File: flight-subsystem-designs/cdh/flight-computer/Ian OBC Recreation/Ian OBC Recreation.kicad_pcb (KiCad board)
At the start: 4 copper layers, 90 x 96 mm, 42 parts, among them J8 Conn_02x26_Odd_Even, Q1 AON6411, Q2 AON6411, U1 BEAGLEBONEBLACK, U2 TPS2400DBVR, U3 TCAN337G, U4 MCP7940N-xSN, U5 ADM3485EARZ, U6 MAX706RESA+T, U7 TMP36xS, U8 TPS2400DBVR

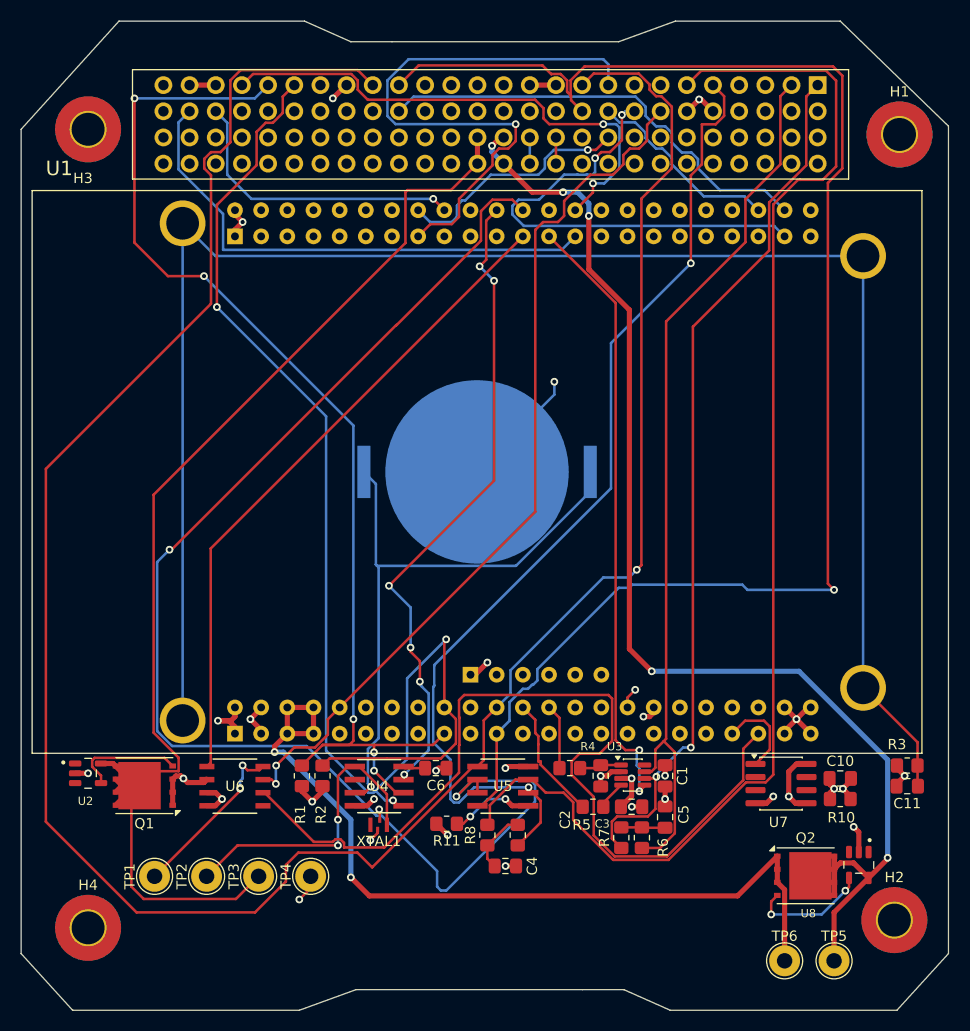
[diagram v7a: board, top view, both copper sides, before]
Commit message: Not LibreCube Friendly, Holes Removed
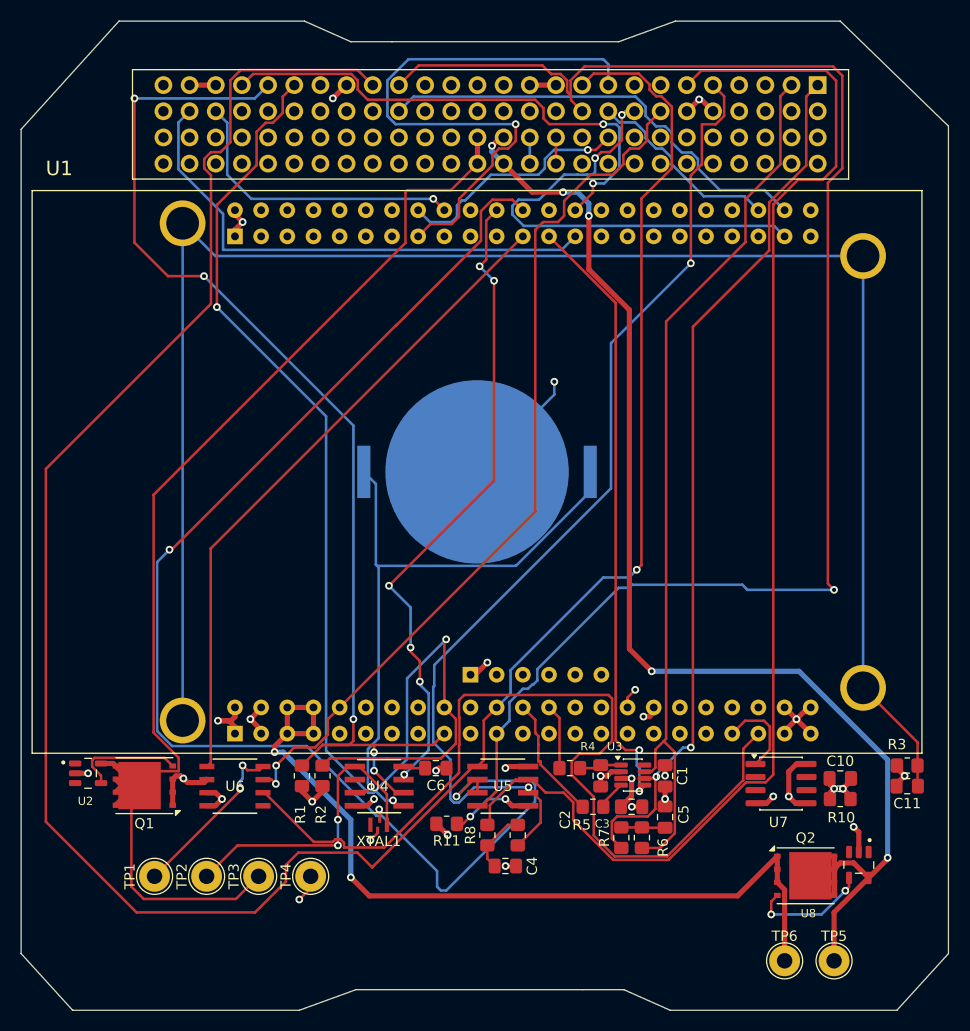
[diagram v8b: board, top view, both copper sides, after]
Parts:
- removed H1, H2, H3, H4: MountingHole_Pad, MountingHole:MountingHole_3.2mm_M3_Pad_TopBottom
